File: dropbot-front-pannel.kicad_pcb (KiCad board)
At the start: 4 copper layers, 108.3 x 68.8 mm, 28 parts, among them P1 SFM-105-02-L-D-A, P10 CONN_01X02, P11 USB_A, P12 USB_B, P13 CONN_01X01, P14 CONN_01X01, P15 CONN_01X01, P2 SFM-125-02-L-D-A, P3 TFM-125-02-L-DH, P4 SFM-125-02-L-D-A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

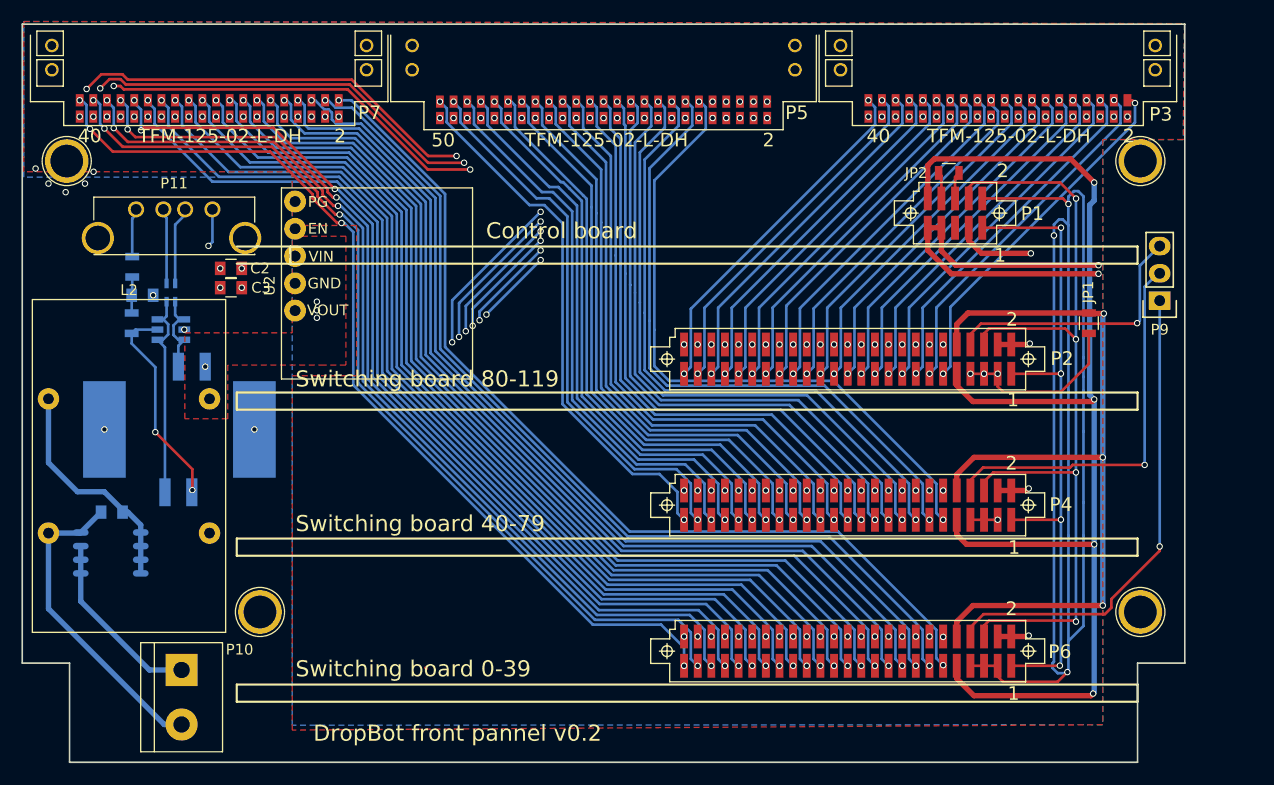
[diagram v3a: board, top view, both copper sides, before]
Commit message: Finish routing all nets, move components to front of board
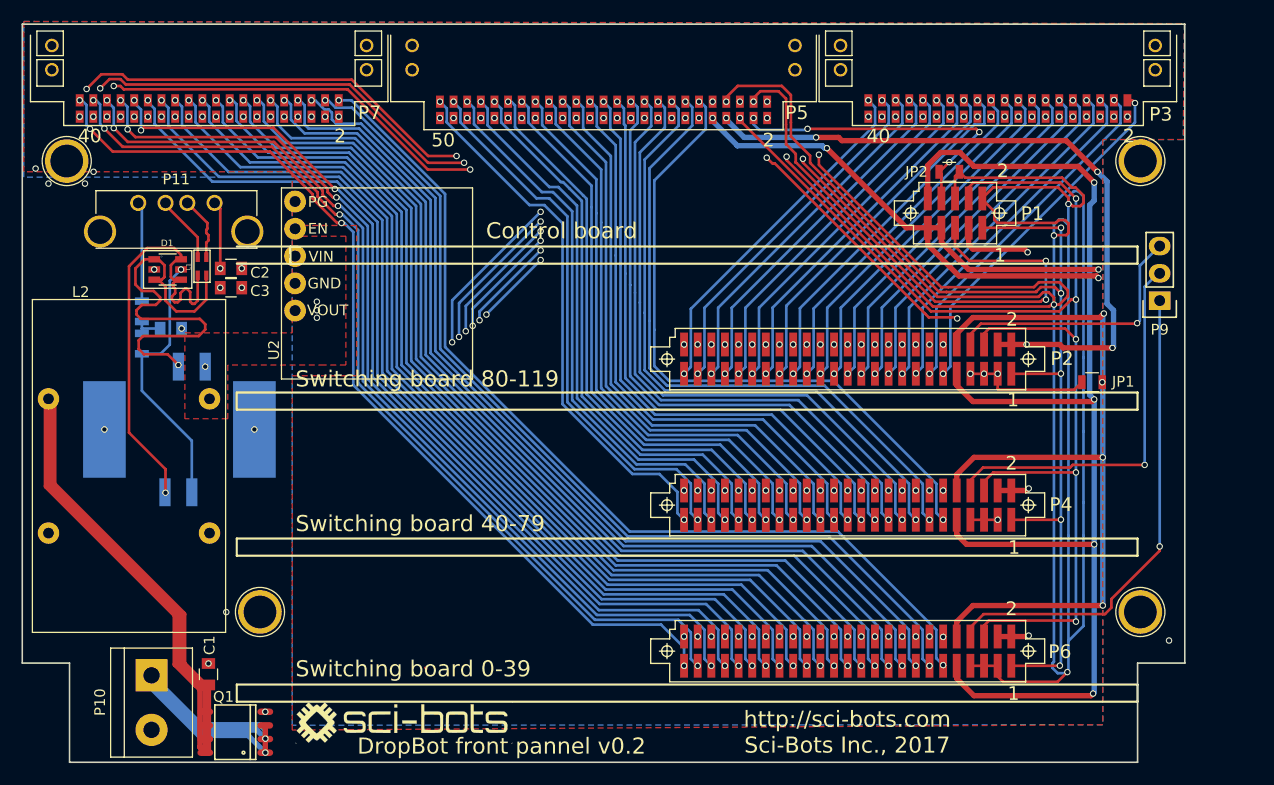
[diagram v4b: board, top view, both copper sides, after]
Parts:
- added G***: LOGO, WheelerLab:SCI-BOTS-LOGO, F.Cu at (81.4, 96.3)
- C1, D1, L1, Q1: moved to F.Cu
- moved Q1 20.3 mm to (65.7, 97.2)
- moved C1 17.6 mm to (63.2, 91.8), turned to 90 degrees
- moved D1 5.61 mm to (59.4, 54.1)
- moved JP1 5.51 mm to (145.5, 64.6), turned to 0 degrees
- moved FB2 4.25 mm to (57.0, 58.0)
- moved C4 4.08 mm to (59.7, 59.6)
- moved L1 3.80 mm to (62.6, 53.8)
- moved P10 2.84 mm to (57.9, 91.9)
- moved FB1 2.12 mm to (57.0, 61.0)
- moved P11 0.63 mm to (60.2, 47.9)
- moved JP2 0.12 mm to (132.2, 45.0)
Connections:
- net Net-(P5-Pad1) renamed CH-X2
- net Net-(P5-Pad2) renamed CH-X1
- L1 pad 1: Net-(D1-Pad1) -> Net-(D1-Pad4)
- L1 pad 2: Net-(L1-Pad2) -> D-
- L1 pad 3: Net-(L1-Pad3) -> D+
- L1 pad 4: Net-(D1-Pad4) -> Net-(D1-Pad1)
- P11 pad 2: Net-(L1-Pad3) -> D-
- P11 pad 3: Net-(L1-Pad2) -> D+
- P5 pad 10: Net-(P5-Pad10) -> +12V
- P5 pad 3: Net-(P5-Pad3) -> CUR_SENSE
- P5 pad 4: Net-(P5-Pad4) -> HV_OE
- P5 pad 5: Net-(P5-Pad5) -> GND
- P5 pad 6: Net-(P5-Pad6) -> SCL
- P5 pad 7: Net-(P5-Pad7) -> SDA
- P5 pad 8: Net-(P5-Pad8) -> +3.3V
- P5 pad 9: Net-(P5-Pad9) -> GND
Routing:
- net GND: track 177.0 -> 296.6 mm, vias 12 -> 17
- net Net-(C1-Pad1): track 21.6 -> 119.5 mm
- net +3.3V: track 21.6 -> 83.1 mm, vias 7 -> 11
- net CUR_SENSE: track 0.00 -> 53.4 mm, vias 0 -> 3
- net SDA: track 61.9 -> 105.1 mm, vias 4 -> 6
- net SCL: track 83.8 -> 123.1 mm, vias 4 -> 6
- net Net-(D1-Pad1): track 8.73 -> 41.7 mm, vias 0 -> 1
- net HV_OE: track 2.48 -> 30.3 mm, vias 0 -> 4
- net +12V_SUPPLY: track 17.2 -> 43.7 mm, vias 0 -> 2
- net CHASIS_GND: track 43.9 -> 18.3 mm, vias 9 -> 12
- net (no net): track 0.14 -> 24.2 mm, vias 0 -> 2
- net +12V: track 37.7 -> 61.7 mm, vias 3 -> 5
- net Net-(D1-Pad4): track 20.6 -> 41.7 mm, vias 0 -> 1
- net Net-(L1-Pad2): track 6.79 -> 0.00 mm
- net Net-(L1-Pad3): track 6.53 -> 0.00 mm
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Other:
- board text added: "http://sci-bots.com Sci-Bots Inc., 2017"

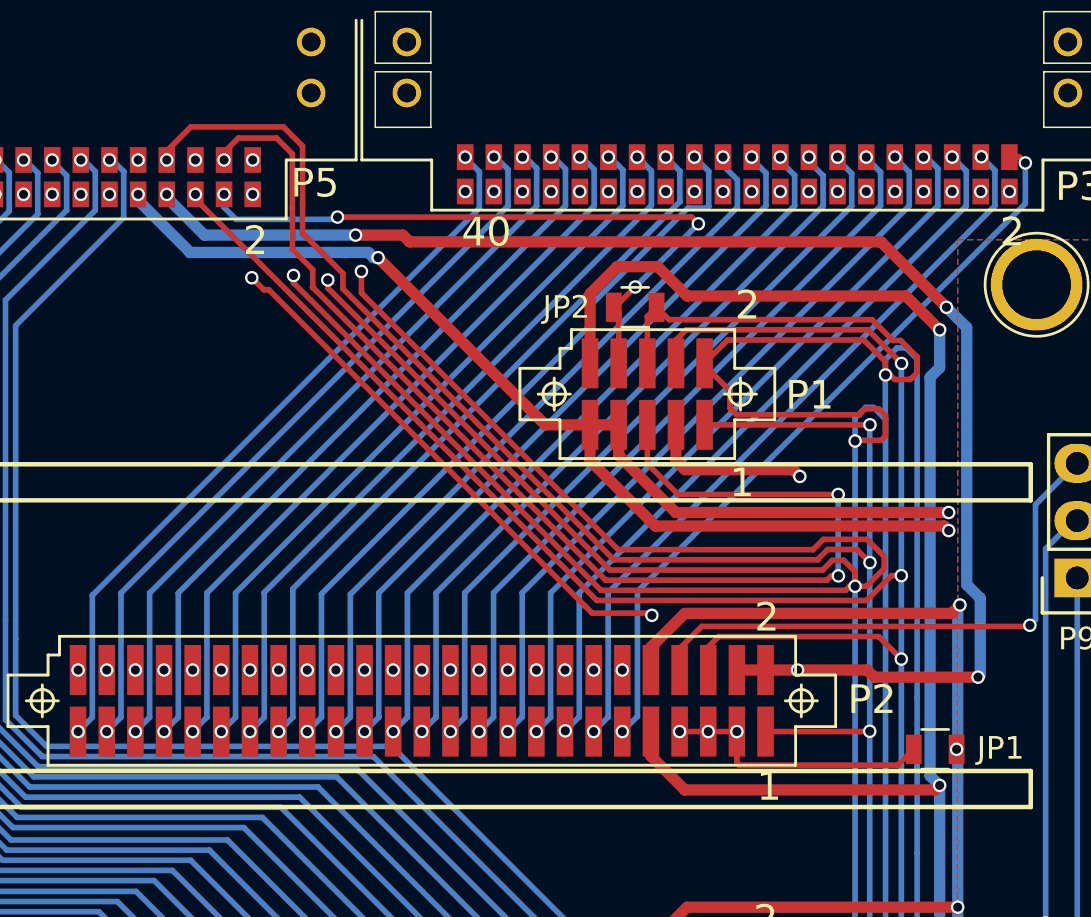
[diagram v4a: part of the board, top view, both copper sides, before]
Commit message: Fix control board connector to match v3.1
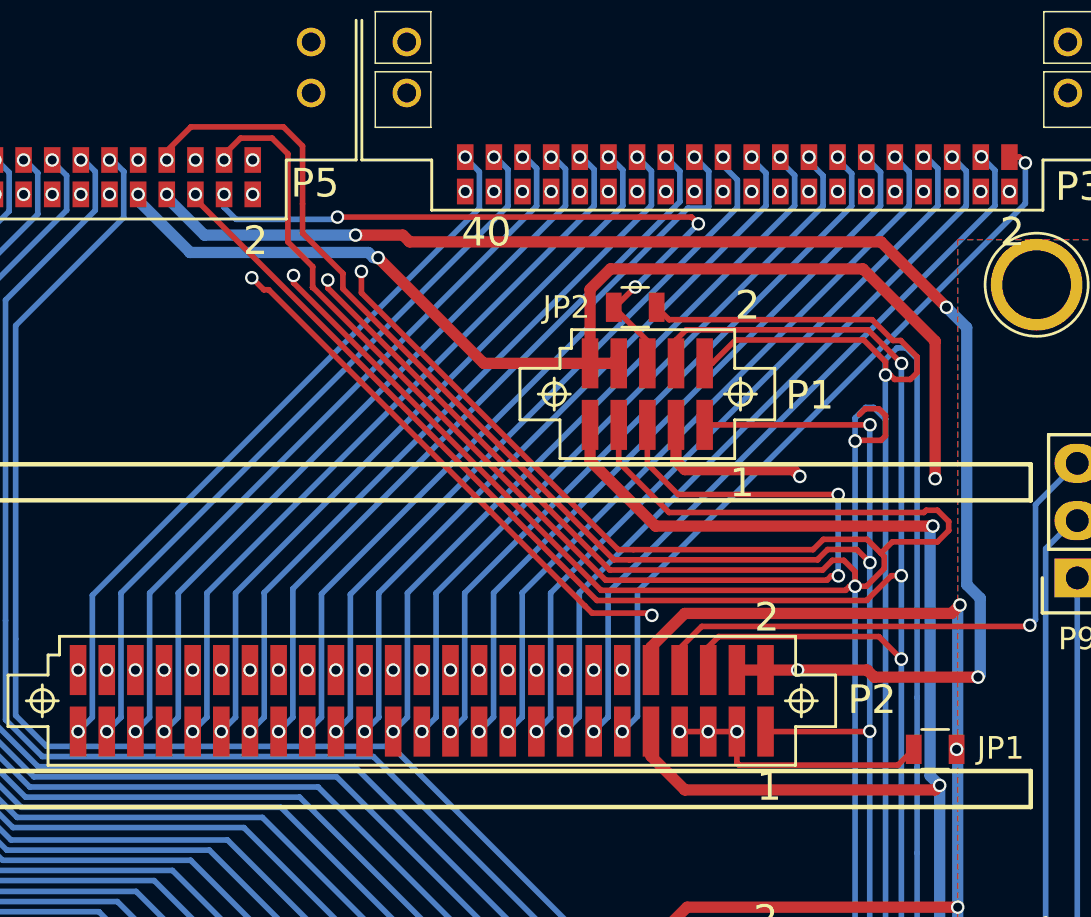
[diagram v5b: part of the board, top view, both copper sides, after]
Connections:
- P1 pad 10: HVAC -> +12V
- P1 pad 6: GND -> HV_OE
- P1 pad 7: +12V -> GND
- P1 pad 8: HV_OE -> +12V
- P1 pad 9: +12V -> HVAC
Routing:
- net HVAC: track 112.0 -> 101.0 mm
- net +12V: track 61.7 -> 51.1 mm, vias 5 -> 4
- net GND: track 296.6 -> 307.0 mm
- net HV_OE: track 30.3 -> 31.2 mm

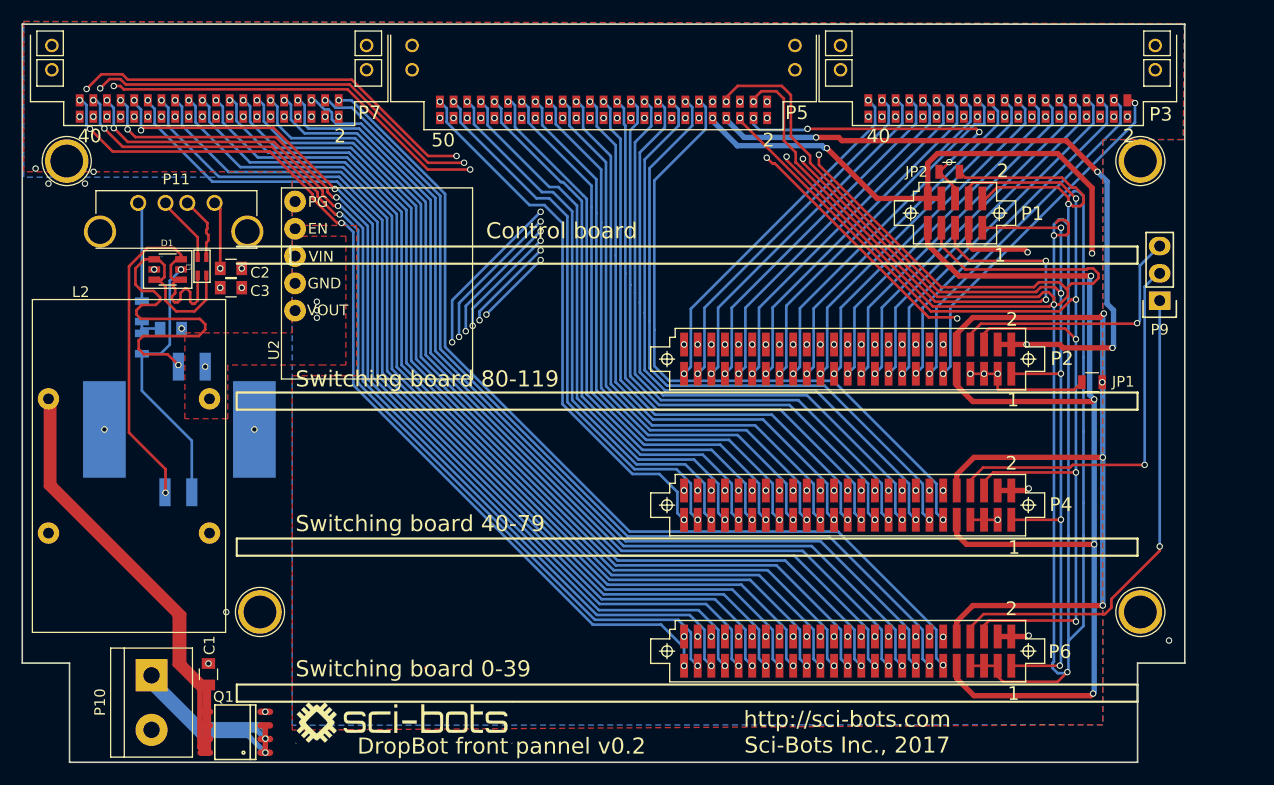
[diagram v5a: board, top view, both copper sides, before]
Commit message: Remove usb passthrough, fix SMT connector...
* remove usb passthrough
* fix SMT connector footprints (missing holes)
* remove USB passthrough (now on control board)
* move power connector to top of board
* increase height of cutouts in bottom corners
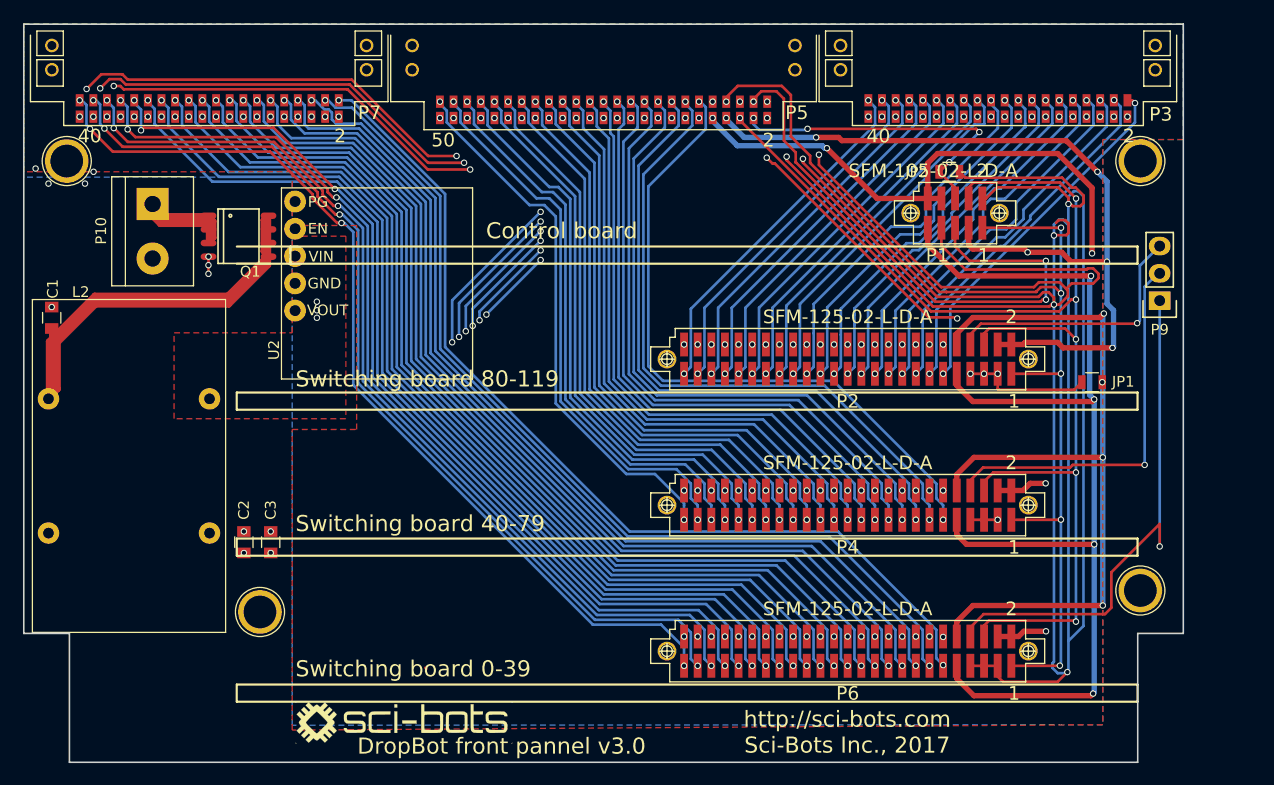
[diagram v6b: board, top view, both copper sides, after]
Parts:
- removed C4: 0.1uF, Capacitors_SMD:C_0805
- removed D1: WE-TVS_824015, WheelerLab:wurth-WE-TVS_SOT23-6L
- removed FB1, FB2: 600 Ohm@100MHz, Resistors_SMD:R_0805
- removed L1: 90 Ohm@100MHz, WheelerLab:wurth-WE-CNSW_0805
- removed P11: USB_A, WheelerLab:UE27AE54100
- removed P12: USB_B, WheelerLab:1734517-1
- moved Q1 46.2 mm to (66.0, 51.0), turned to 270 degrees
- moved P10 43.9 mm to (58.0, 48.0)
- moved C1 36.3 mm to (48.6, 58.6)
- moved C2 25.5 mm to (66.5, 79.5), turned to 270 degrees
- moved C3 24.0 mm to (69.0, 79.5), turned to 270 degrees
- moved P14 2.00 mm to (150.0, 84.0)
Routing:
- net Net-(D1-Pad1): track 41.7 -> 0.00 mm, vias 1 -> 0
- net Net-(D1-Pad4): track 41.7 -> 0.00 mm, vias 1 -> 0
- net Net-(D1-Pad5): track 25.4 -> 0.00 mm, vias 1 -> 0
- net Net-(C1-Pad1): track 119.5 -> 96.7 mm
- net +12V_SUPPLY: track 43.7 -> 24.1 mm, vias 2 -> 0
- net +3.3V: track 83.1 -> 94.6 mm
- net Net-(FB2-Pad2): track 9.29 -> 0.00 mm
- net GND: track 307.0 -> 300.1 mm, vias 17 -> 14
- net D-: track 6.29 -> 0.00 mm
- net D+: track 6.03 -> 0.00 mm
- net CHASIS_GND: track 18.3 -> 13.2 mm, vias 12 -> 10
- net RST1: track 46.2 -> 50.4 mm
- net Net-(C4-Pad2): track 2.80 -> 0.00 mm
- net HVOUT99: track 33.1 -> 34.7 mm
- net HVOUT101: track 33.1 -> 34.2 mm
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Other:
- board size 108.3 x 68.8 mm -> 108 x 68.8 mm
- board text added: "DropBot front pannel v3.0"
- board text removed: "DropBot front pannel v0.2"

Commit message: label +12V and G on power connector
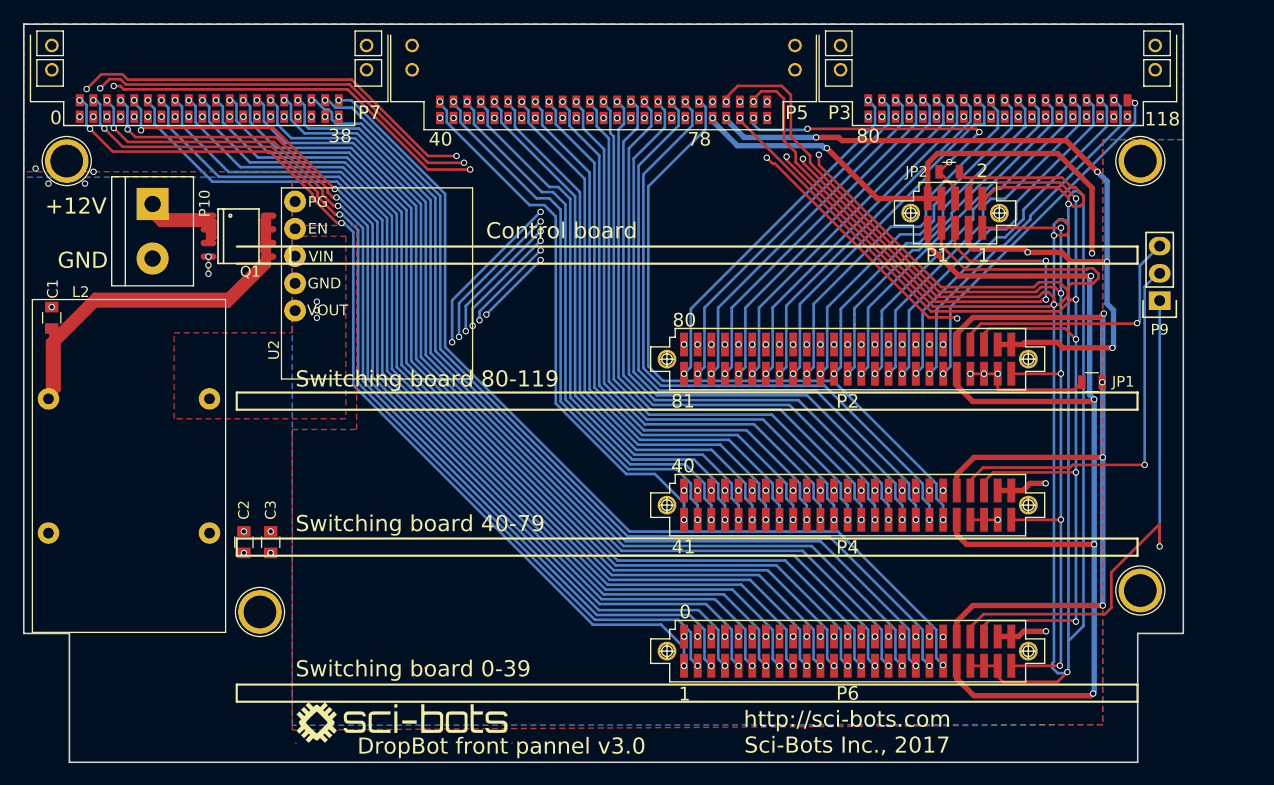
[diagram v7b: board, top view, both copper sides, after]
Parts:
- P1: footprint WheelerLab:SFM-105-02-XXX-D-A -> SFM-105-02-XXX-D-A
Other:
- board text added: "+12V"
- board text added: "GND"
